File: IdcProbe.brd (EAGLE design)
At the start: 50 x 80 mm, 78 parts, among them P1 BANANA_SOCKETVERTICAL, P2 BANANA_SOCKETVERTICAL, Q1 PMV45EN, U1 TPS65131RGET, U2 NCP361MUTBG, U4 TL074D, X3 R141426

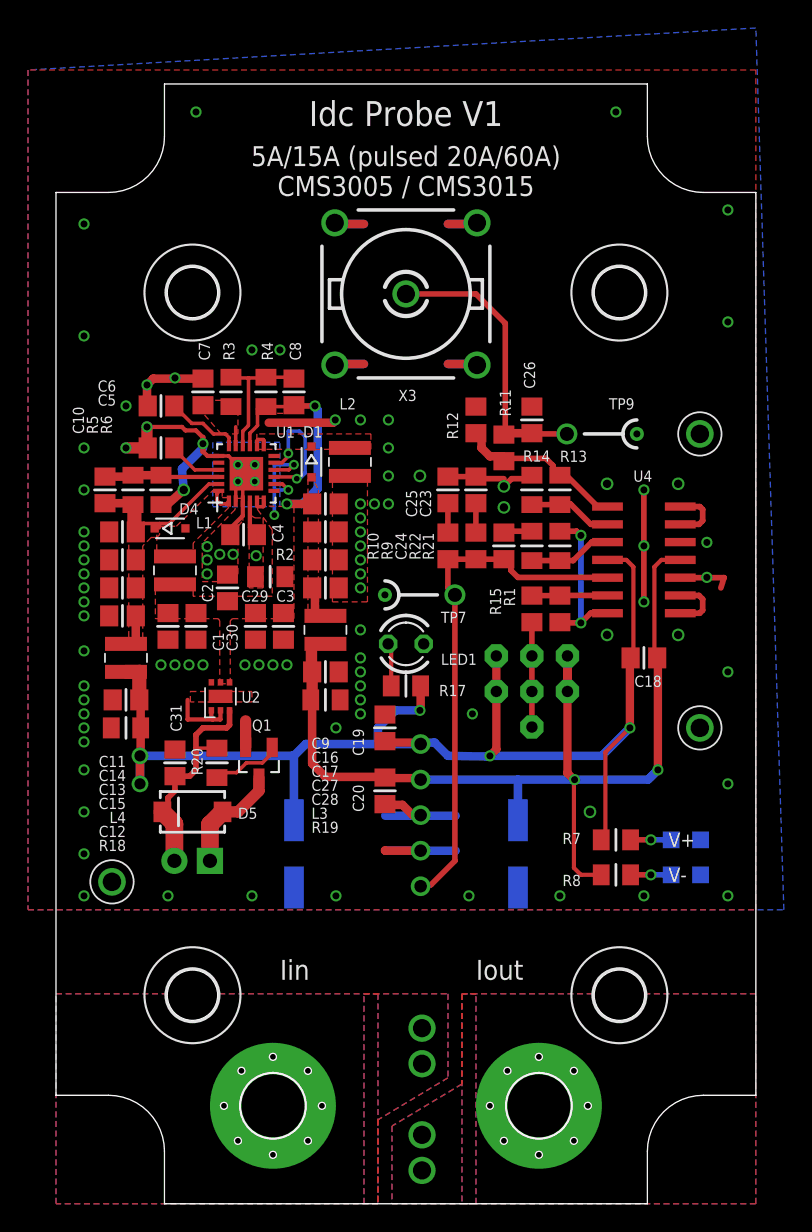
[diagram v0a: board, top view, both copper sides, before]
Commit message: Update
Added fuse.
Renumbered schematic.
Created pdf and gerber for review.
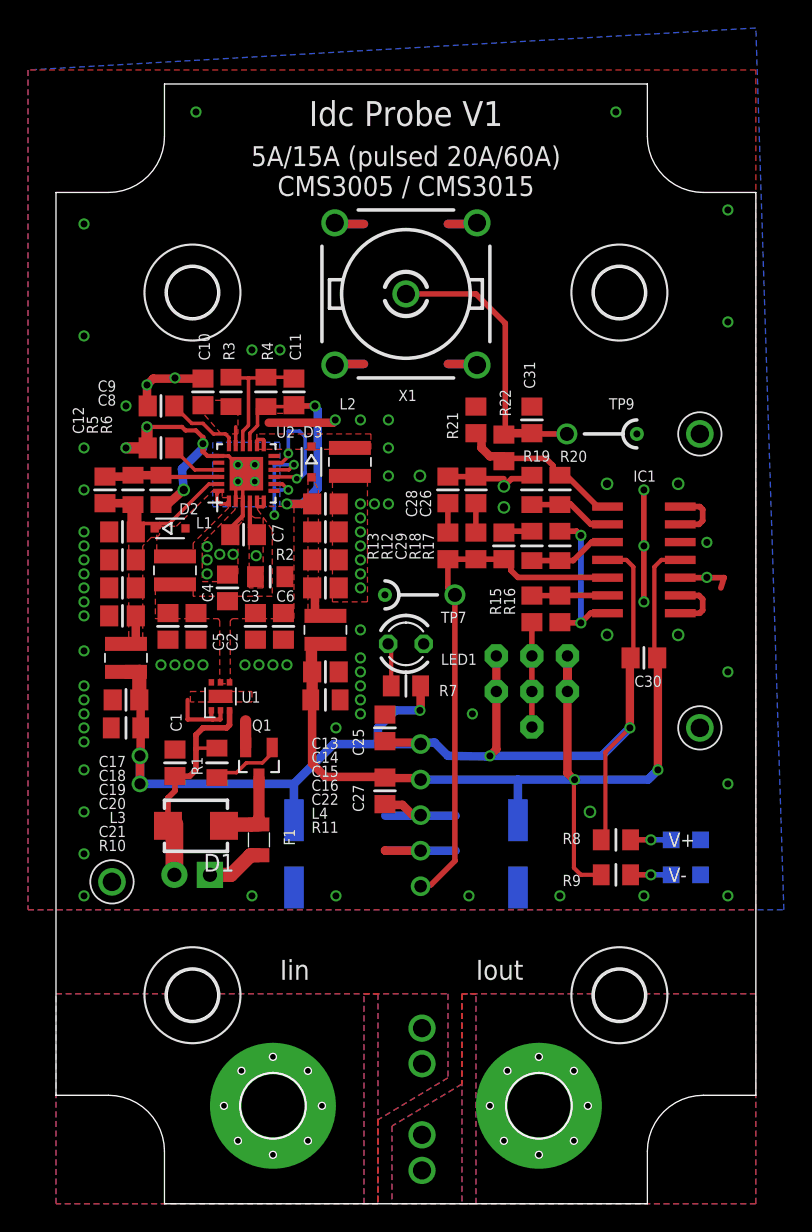
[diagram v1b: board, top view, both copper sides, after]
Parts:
- removed D5: SMAJ5.0A, Jeroen:SMA-DIODE
- added D3: Schottky 1A 20V, diode:SOD323-R
- added F1: 0.5AT, dp_devices:PTC0805
- C1: value 4.7uF 25V X5R -> 1uF 25V X5R
- C10: value (none) -> 220nF
- C11, C12, C28: value 4.7uF 25V X5R -> (none)
- C18, C19, C20, C4: value 100nF -> 4.7uF 25V X5R
- C2, C27, C3: value 4.7uF 25V X5R -> 100nF
- C21, C22: value 47uF (EEEFK1V470P) -> 4.7uF 25V X5R; device rcl:PANASONIC_D -> rcl:C0805
- C23: value 3.3nF / 2.2nF -> 47uF (EEEFK1V470P); device rcl:C0805 -> rcl:PANASONIC_D
- C24: value (none) -> 47uF (EEEFK1V470P); device rcl:C0805 -> rcl:PANASONIC_D
- C25: value (none) -> 100nF
- C26: value (none) -> 3.3nF / 2.2nF
- C29: value 100nF -> (none)
- C31: value 1uF 25V X5R -> (none)
- C5: value 10nF 16V X7R -> 4.7uF 25V X5R
- C6: value 4.7nF 50V C0G -> 4.7uF 25V X5R
- C7: value 220nF -> 100nF
- C8: value (none) -> 10nF 16V X7R
- C9: value 4.7uF 25V X5R -> 4.7nF 50V C0G
- D1: value Schottky 1A 20V -> SMAJ12CA; device diode:SOD323-R -> Jeroen:SMA_NOPOL
- LED1, LED2, LED3: value (none) -> Green
- R1: value 1K -> 1k; device rcl:R0805 -> rcl:R0805I
- R10: value (none) -> 10k; device rcl:R0805 -> rcl:R0805I
- R11: value 0 -> 10k; device rcl:R0805 -> rcl:R0805I
- R12: value 100k -> 15 / 33
- R13: value 10k -> (none); device rcl:R0805I -> rcl:R0805
- R14: value (none) -> 100k; device rcl:R0805I -> Jeroen:3386-MULTI
- R16: value 100k -> 1K; device Jeroen:3386-MULTI -> rcl:R0805
- R17: value 3.9k -> 10k
- R18, R19: value 10k -> (none)
- R20: value 1k -> 10k
- R21: value 10k -> 100k; device rcl:R0805I -> rcl:R0805
- R22: value (none) -> 0; device rcl:R0805I -> rcl:R0805
- R9: value 15 / 33 -> 3.9k; device rcl:R0805 -> rcl:R0805I
- U1: value TPS65131RGET -> NCP361MUTBG; device Jeroen:QFN50P400X400X100-25N -> Jeroen:UDFN6_2X2
- U2: value NCP361MUTBG -> TPS65131RGET; device Jeroen:UDFN6_2X2 -> Jeroen:QFN50P400X400X100-25N
- moved C18 37.9 mm to (4.75, 46.0)
- moved C31 35.4 mm to (34.0, 56.0), turned to 270 degrees
- moved C30 32.1 mm to (42.0, 39.0), turned to 180 degrees
- moved R18 31.8 mm to (34.0, 47.0), turned to 270 degrees
- moved R20 31.3 mm to (36.0, 51.0)
- moved C23 29.1 mm to (17.0, 25.0), flipped to the bottom, turned to 90 degrees
- moved D1 27.3 mm to (10.0, 27.0), turned to 180 degrees
- moved R1 26.9 mm to (11.5, 31.5), turned to 90 degrees
- moved R10 26.4 mm to (5.00, 34.0), turned to 0 degrees
- moved R9 25.5 mm to (40.0, 23.5), turned to 0 degrees
- moved C20 22.5 mm to (4.75, 42.0), turned to 180 degrees
- moved R11 22.1 mm to (19.2, 36.0), turned to 0 degrees
- moved C24 22.0 mm to (33.0, 25.0), flipped to the bottom
- moved C19 21.2 mm to (4.75, 44.0), turned to 180 degrees
- moved R19 21.0 mm to (34.0, 51.0), turned to 270 degrees
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- renumbered D4 to D2, LD2 to LED2, LD3 to LED3, U$1 to H1, U4 to IC1, X3 to X1
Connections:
- new net N$21: F1.2, J1.1
- net CN: now also C9.1, U2.18; no longer C6.1, U1.18
- net CP: now also C8.1, U2.21; no longer C5.1, U1.21
- net FBN: now also C11.1, U2.16; no longer C8.1, U1.16
- net FBP: now also C12.2, U2.22; no longer C10.2, U1.22
- net GND: now also C10.2, C18.2, C19.2, C20.2, C21.2, C22.2, C23.-, C24.+, C27.1, C28.1, C29.1, C31.1, C8.2, R10.1, R11.2, R19.1, R21.1, U1.1, U1.7, U2.11, U2.19, U2.25, U2.3, U2.9; no longer C11.2, C12.2, C19.1, C20.1, C21.-, C22.+, C23.1, C24.1, C27.2, C28.2, C29.2, C30.2, C31.2, R12.1, R14.1, R19.2, R22.1, U1.11, U1.19, U1.25, U1.3, U1.9, U2.1, U2.7
- net INP: now also U2.1, U2.24; no longer U1.1, U1.24
- net N$1: now also R8.1; no longer R7.1
- net N$10: now also C28.2, R13.2; no longer C25.2, R10.2
- net N$11: now also R20.2, R21.2, R22.1; no longer R11.1, R12.2, R13.2
- net N$12: now also C31.2, R22.2; no longer C26.2, R11.2
- net N$13: now also C29.2, R12.1, R13.1; no longer C24.2, R10.1, R9.1
- net N$14: now also R19.2, R20.1; no longer R13.1, R14.2
- net N$15: now also R14.2, R14.5, R14.7; no longer R16.2, R16.5, R16.7
- net N$16: now also R7.1; no longer R17.1
- net N$17: now also C1.1, D1.2, R1.2, U1.3; no longer C31.1, D5.C, R20.2, U2.3
- net N$18: now also D1.1, F1.1; no longer D5.A, J1.1
- net N$19: now also R1.1; no longer R20.1
- net N$2: now also R9.2; no longer R8.2
- net N$20: now also R17.2, R18.2; no longer R21.2, R22.2
- net N$3: now also R16.2, R17.1; no longer R1.2, R21.1
- net N$4: now also R16.1; no longer R1.1
- net N$9: now also C26.2, R12.2; no longer C23.2, R9.2
- net OUTN: now also D3.C, U2.13, U2.14; no longer D1.C, U1.13, U1.14
- net RV+: now also C12.1, C17.1, C18.1, C19.1, C20.1, L3.1, U2.23; no longer C10.1, C11.1, C13.1, C14.1, C15.1, L4.1, U1.23
- net RV-: now also C11.2, C13.1, C14.1, C15.1, D3.A, L4.1, U2.15; no longer C17.1, C27.1, C8.2, C9.1, D1.A, L3.1, U1.15
- net V+: now also C21.1, C23.+, C25.2, C30.2, L3.2, R10.2, R14.3, R14.6, R8.2; no longer C12.1, C18.2, C19.2, C21.+, L4.2, R16.3, R16.6, R17.2, R18.2
- net V-: now also C22.1, C24.-, C27.2, C30.1, L4.2, R11.1, R14.1, R14.4, R9.1; no longer C18.1, C20.2, C22.-, C28.1, L3.2, R16.1, R16.4, R19.1, R8.1
- net VI: now also C4.1, C5.1, C6.1, U1.4, U2.10, U2.6, U2.8; no longer C1.1, C29.1, C30.1, U1.10, U1.6, U1.8, U2.4
- net VIN: now also C7.1, U2.4; no longer C4.1, U1.4
- net VREF: now also C10.1, U2.17; no longer C7.1, U1.17
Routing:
- net N$21: track 0.00 -> 4.08 mm
- net V+: track 92.1 -> 90.9 mm
- net N$18: track 7.99 -> 7.31 mm
- net GND: vias 97 -> 96
